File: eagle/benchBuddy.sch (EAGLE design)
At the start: 74 parts, among them IC2 TLC274D, IC3 LM334Z, IC4 LM324D, IC5 LM324D, J1 12V_DC, Q1 600mA/40V, U1 LP2983AIM5-1.0/NOPB, U2 LP2985-10DBVR

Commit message: Added all parts. Schematic finished. Consider Rev 1.0
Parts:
- added C10, C12, C14, C9: 10uF, rcl:C-USC0805
- added C11, C8: 0.1uF, rcl:C-USC0805
- added D1, D2, D3: (no value), SparkFun-LED:LED3MM
- added F1: 4A It, lab07lib:FUSE
- added F2, F3: 1.5A It, lab07lib:FUSE
- added J4, J8: GND, lab07lib:FAT-WIRE-TERM
- added J5: 3.3V, lab07lib:FAT-WIRE-TERM
- added J6: 5V, lab07lib:FAT-WIRE-TERM
- added J7: 12V, lab07lib:FAT-WIRE-TERM
- added J9: 0-10V, lab07lib:FAT-WIRE-TERM
- added PS1, PS2: P78E05-1000, P78E05-1000:P78E05-1000
- added R31, R32, R33: (no value), rcl:R-US_R1206
- added U3: 3V3REG, PowerManagementParts:3V3REG
- renumbered JP3 to J3, U$3 to J2
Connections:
- new net 3.3V: C10.1, C11.1, D3.A, J5.P$1, U3.VOUT
- new net 5V: C8.1, C9.1, D2.A, J3.6, J6.P$1, PS2.+VOUT/GND
- new net N$4: D1.A
- new net N$41: D1.C, R31.2
- new net N$42: D2.C, R32.2
- new net N$43: D3.C, R33.2
- new net N$44: F1.P$2, U$2.COM
- new net N$45: IC4B.OUT, LED3.A
- new net N$46: IC4C.OUT, LED4.A
- new net N$47: IC4D.OUT, LED5.A
- new net N$48: F2.P$1, PS1.+VOUT/GND
- new net N$49: C12.1, F2.P$2, U3.INPUT
- new net N$7: F3.P$2, PS2.+VIN
- net 10VOLTS: no longer J3.6
- net GND: now also C10.2, C11.2, C12.2, C14.2, C8.2, C9.2, J4.P$1, J8.P$1, PS1.GND/-VOUT, PS2.GND/-VOUT, R31.1, R32.1, R33.1, U3.GND
- net N$3: now also F1.P$1; no longer U$2.COM
- net VCC: now also J9.P$1
- net VIN: now also C14.1, F3.P$1, J7.P$1, PS1.+VIN
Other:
- note added: "1.0"
- note added: "3.3V @ 1A Supply"
- note added: "5V @ 1A Supply"
- note added: "Indicator LEDs"
- note added: "Mark Gilliland EENG 393 - ICE Field Session"
- note removed: "0.1"
- note removed: "Mark Gilliland 9/30/2019 EENG 393 - ICE Field Session"
- moved on the sheet: J1, U$2

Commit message: Basic dimensions and mechanical layout of board
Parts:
- renumbered U$2 to SW4
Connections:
- removed net N$4: D1.A
- net VIN: now also D1.A
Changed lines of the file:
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@@
 <part name="GND17" library="supply1" library_urn="urn:adsk.eagle:library:371" deviceset="GND" device=""/>
 <part name="U$1" library="lab07lib" deviceset="LT3080" device=""/>
-<part name="U$2" library="lab07lib" deviceset="EG2362" device=""/>
+<part name="SW4" library="lab07lib" deviceset="EG2362" device=""/>
 <part name="KK1" library="heatsink" library_urn="urn:adsk.eagle:library:236" deviceset="SK104-PAD" device="" package3d_urn="urn:adsk.eagle:package:14201/1"/>
 <part name="TP1" library="testpad" library_urn="urn:adsk.eagle:library:385" deviceset="TP" device="TP13R" package3d_urn="urn:adsk.eagle:package:27967/1"/>
@@
 </instance>
 <instance part="U$1" gate="G$1" x="177.8" y="185.42" smashed="yes"/>
-<instance part="U$2" gate="G$1" x="45.72" y="185.42" smashed="yes">
+<instance part="SW4" gate="G$1" x="45.72" y="185.42" smashed="yes">
 <attribute name="NAME" x="38.1" y="190.5" size="1.27" layer="94"/>
 <attribute name="VALUE" x="48.26" y="190.5" size="1.27" layer="94"/>
@@
 <junction x="63.5" y="182.88"/>
 <junction x="76.2" y="182.88"/>
-<pinref part="U$2" gate="G$1" pin="ON2"/>
+<pinref part="SW4" gate="G$1" pin="ON2"/>
 </segment>
 <segment>
@@
 <segment>
 <pinref part="F1" gate="G$1" pin="P$2"/>
-<pinref part="U$2" gate="G$1" pin="COM"/>
+<pinref part="SW4" gate="G$1" pin="COM"/>
 <wire x1="33.02" y1="185.42" x2="38.1" y2="185.42" width="0.1524" layer="91"/>
 </segment>
@@
 </busses>
 <nets>
-<net name="N$4" class="0">
-<segment>
-<pinref part="D1" gate="G$1" pin="A"/>
-<wire x1="45.72" y1="35.56" x2="45.72" y2="40.64" width="0.1524" layer="91"/>
-<pinref part="SUPPLY11" gate="G$1" pin="VIN"/>
-<wire x1="45.72" y1="40.64" x2="45.72" y2="38.1" width="0.1524" layer="91"/>
-</segment>
-</net>
 <net name="5V" class="0">
 <segment>
@@
 <wire x1="114.3" y1="20.32" x2="109.22" y2="20.32" width="0.1524" layer="91"/>
 </segment>
-</net>
+<segment>
+<pinref part="D1" gate="G$1" pin="A"/>
+<wire x1="45.72" y1="35.56" x2="45.72" y2="40.64" width="0.1524" layer="91"/>
+<pinref part="SUPPLY11" gate="G$1" pin="VIN"/>
+<wire x1="45.72" y1="40.64" x2="45.72" y2="38.1" width="0.1524" layer="91"/>
+</segment>
+</net>

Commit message: More detailed board layout. Began LED and VU layout
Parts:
- added C13: 0.1uF, rcl:C-USC0805
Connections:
- removed net N$22: C7.1, U2.VOUT
- removed net N$37: C5.1, U1.VOUT
- net 10VOLTS: now also C7.1, U2.VOUT
- net 1VOLT: now also C5.1, U1.VOUT
- net GND: now also C13.2
- net VCC: now also C13.1
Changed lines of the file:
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@@
 <part name="GND27" library="supply1" library_urn="urn:adsk.eagle:library:371" deviceset="GND" device=""/>
 <part name="SUPPLY12" library="SparkFun-PowerSymbols" library_urn="urn:adsk.eagle:library:530" deviceset="VIN" device=""/>
+<part name="C13" library="rcl" library_urn="urn:adsk.eagle:library:334" deviceset="C-US" device="C0805" package3d_urn="urn:adsk.eagle:package:23617/2" value="0.1uF"/>
 </parts>
 <sheets>
@@
 <attribute name="VALUE" x="25.4" y="188.722" size="1.778" layer="96"/>
 </instance>
+<instance part="C13" gate="G$1" x="223.52" y="175.26" smashed="yes">
+<attribute name="NAME" x="224.536" y="175.895" size="1.778" layer="95"/>
+<attribute name="VALUE" x="224.536" y="171.069" size="1.778" layer="96"/>
+</instance>
 </instances>
 <busses>
@@
 <pinref part="GND11" gate="1" pin="GND"/>
 <pinref part="C3" gate="G$1" pin="-"/>
-<wire x1="213.36" y1="162.56" x2="213.36" y2="170.18" width="0.1524" layer="91"/>
+<wire x1="213.36" y1="162.56" x2="213.36" y2="167.64" width="0.1524" layer="91"/>
+<pinref part="C13" gate="G$1" pin="2"/>
+<wire x1="213.36" y1="167.64" x2="213.36" y2="170.18" width="0.1524" layer="91"/>
+<wire x1="223.52" y1="170.18" x2="223.52" y2="167.64" width="0.1524" layer="91"/>
+<wire x1="223.52" y1="167.64" x2="213.36" y2="167.64" width="0.1524" layer="91"/>
+<junction x="213.36" y="167.64"/>
 </segment>
 <segment>
@@
 <wire x1="238.76" y1="182.88" x2="238.76" y2="187.96" width="0.1524" layer="91"/>
 <wire x1="213.36" y1="177.8" x2="213.36" y2="182.88" width="0.1524" layer="91"/>
-<wire x1="213.36" y1="182.88" x2="238.76" y2="182.88" width="0.1524" layer="91"/>
+<wire x1="213.36" y1="182.88" x2="223.52" y2="182.88" width="0.1524" layer="91"/>
 <junction x="238.76" y="182.88"/>
 <pinref part="U$1" gate="G$1" pin="VOUT"/>
+<wire x1="223.52" y1="182.88" x2="238.76" y2="182.88" width="0.1524" layer="91"/>
 <wire x1="213.36" y1="182.88" x2="203.2" y2="182.88" width="0.1524" layer="91"/>
 <junction x="213.36" y="182.88"/>
 <pinref part="J2" gate="G$1" pin="P$1"/>
 <wire x1="238.76" y1="182.88" x2="259.08" y2="182.88" width="0.1524" layer="91"/>
+<pinref part="C13" gate="G$1" pin="1"/>
+<wire x1="223.52" y1="177.8" x2="223.52" y2="182.88" width="0.1524" layer="91"/>
+<junction x="223.52" y="182.88"/>
 </segment>
 <segment>
@@
 <wire x1="246.38" y1="38.1" x2="226.06" y2="38.1" width="0.1524" layer="91"/>
 <label x="226.06" y="38.1" size="1.778" layer="95"/>
+</segment>
+<segment>
+<pinref part="U2" gate="A" pin="VOUT"/>
+<wire x1="243.84" y1="104.14" x2="261.62" y2="104.14" width="0.1524" layer="91"/>
+<pinref part="C7" gate="G$1" pin="1"/>
+<wire x1="261.62" y1="104.14" x2="261.62" y2="101.6" width="0.1524" layer="91"/>
+<junction x="261.62" y="104.14"/>
+<wire x1="261.62" y1="104.14" x2="266.7" y2="104.14" width="0.1524" layer="91"/>
+<label x="264.16" y="104.14" size="1.778" layer="95"/>
 </segment>
 </net>
@@
 <wire x1="243.84" y1="40.64" x2="226.06" y2="40.64" width="0.1524" layer="91"/>
 <label x="226.06" y="40.64" size="1.778" layer="95"/>
+</segment>
+<segment>
+<pinref part="C5" gate="G$1" pin="1"/>
+<wire x1="261.62" y1="127" x2="261.62" y2="129.54" width="0.1524" layer="91"/>
+<pinref part="U1" gate="A" pin="VOUT"/>
+<wire x1="261.62" y1="129.54" x2="243.84" y2="129.54" width="0.1524" layer="91"/>
+<wire x1="261.62" y1="129.54" x2="266.7" y2="129.54" width="0.1524" layer="91"/>
+<junction x="261.62" y="129.54"/>
+<label x="264.16" y="129.54" size="1.778" layer="95"/>
 </segment>
 </net>
@@
 </segment>
 </net>
-<net name="N$22" class="0">
-<segment>
-<pinref part="U2" gate="A" pin="VOUT"/>
-<wire x1="243.84" y1="104.14" x2="261.62" y2="104.14" width="0.1524" layer="91"/>
-<pinref part="C7" gate="G$1" pin="1"/>
-<wire x1="261.62" y1="104.14" x2="261.62" y2="101.6" width="0.1524" layer="91"/>
-</segment>
-</net>
-<net name="N$37" class="0">
-<segment>
-<pinref part="C5" gate="G$1" pin="1"/>
-<wire x1="261.62" y1="127" x2="261.62" y2="129.54" width="0.1524" layer="91"/>
-<pinref part="U1" gate="A" pin="VOUT"/>
-<wire x1="261.62" y1="129.54" x2="243.84" y2="129.54" width="0.1524" layer="91"/>
-</segment>
-</net>

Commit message: Most components in final position
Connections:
- net 10VOLTS: now also J3.6
- net 5V: no longer J3.6
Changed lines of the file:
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@@
 <label x="264.16" y="104.14" size="1.778" layer="95"/>
+</segment>
+<segment>
+<pinref part="J3" gate="A" pin="6"/>
+<wire x1="152.4" y1="55.88" x2="175.26" y2="55.88" width="0.1524" layer="91"/>
+<label x="167.64" y="55.88" size="1.778" layer="95"/>
 </segment>
 </net>
@@
 </segment>
 </net>
-<net name="5V" class="0">
-<segment>
-<pinref part="J3" gate="A" pin="6"/>
-<wire x1="152.4" y1="55.88" x2="175.26" y2="55.88" width="0.1524" layer="91"/>
-<label x="172.72" y="55.88" size="1.778" layer="95"/>
-</segment>
-</net>

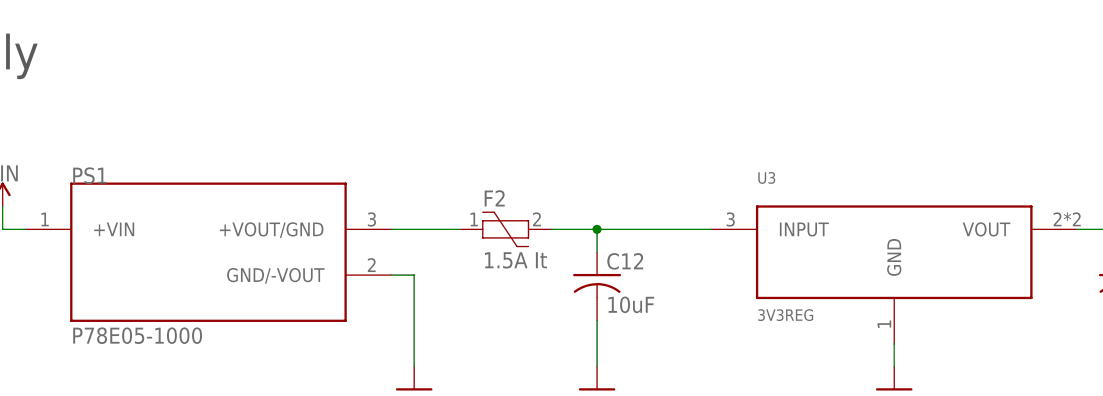
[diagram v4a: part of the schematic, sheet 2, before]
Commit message: Added mini heatsinks for T220 Packages. Also more work on layout
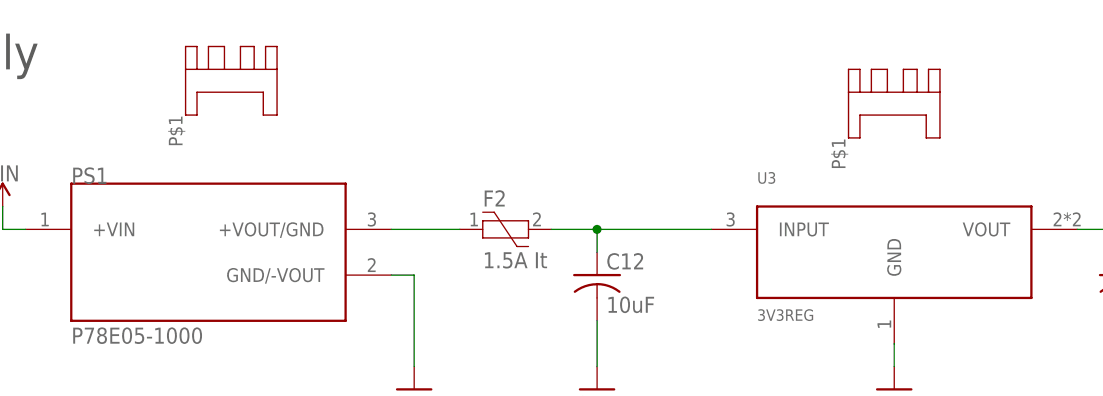
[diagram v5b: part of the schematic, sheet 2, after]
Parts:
- added U$2, U$3: HEATSINK_MINI, lab07lib:HEATSINK_MINI
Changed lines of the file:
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@@
 <part name="SUPPLY12" library="SparkFun-PowerSymbols" library_urn="urn:adsk.eagle:library:530" deviceset="VIN" device=""/>
 <part name="C13" library="rcl" library_urn="urn:adsk.eagle:library:334" deviceset="C-US" device="C0805" package3d_urn="urn:adsk.eagle:package:23617/2" value="0.1uF"/>
+<part name="U$2" library="lab07lib" deviceset="HEATSINK_MINI" device=""/>
+<part name="U$3" library="lab07lib" deviceset="HEATSINK_MINI" device=""/>
 </parts>
 <sheets>
@@
 <attribute name="VALUE" x="106.68" y="23.114" size="1.778" layer="96" align="center-right"/>
 </instance>
+<instance part="U$2" gate="G$1" x="66.04" y="198.12" smashed="yes"/>
+<instance part="U$3" gate="G$1" x="139.7" y="195.58" smashed="yes"/>
 </instances>
 <busses>

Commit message: Board mostly routed! Added heatsink 3.3V version
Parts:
- U3: value 3V3REG -> 3V3REG-HEATSINK; device PowerManagementParts:3V3REG -> lab07lib:3V3REG-HEATSINK
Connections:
- net I_SET_MICRO: now also J3.4; no longer J3.3
- net VCC: now also J3.3; no longer J3.4
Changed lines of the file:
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@@
 <part name="D2" library="SparkFun-LED" library_urn="urn:adsk.eagle:library:529" deviceset="LED" device="3MM" package3d_urn="urn:adsk.eagle:package:39361/1"/>
 <part name="D3" library="SparkFun-LED" library_urn="urn:adsk.eagle:library:529" deviceset="LED" device="3MM" package3d_urn="urn:adsk.eagle:package:39361/1"/>
-<part name="U3" library="PowerManagementParts" deviceset="3V3REG" device="" package3d_urn="urn:adsk.eagle:package:43439/1"/>
+<part name="U3" library="lab07lib" deviceset="3V3REG" device="-HEATSINK"/>
 <part name="R31" library="rcl" library_urn="urn:adsk.eagle:library:334" deviceset="R-US_" device="R1206" package3d_urn="urn:adsk.eagle:package:23540/2"/>
 <part name="R32" library="rcl" library_urn="urn:adsk.eagle:library:334" deviceset="R-US_" device="R1206" package3d_urn="urn:adsk.eagle:package:23540/2"/>
@@
 </segment>
 <segment>
-<pinref part="J3" gate="A" pin="4"/>
-<wire x1="152.4" y1="50.8" x2="175.26" y2="50.8" width="0.1524" layer="91"/>
-<label x="170.18" y="50.8" size="1.778" layer="95"/>
+<pinref part="J3" gate="A" pin="3"/>
+<wire x1="152.4" y1="48.26" x2="167.64" y2="48.26" width="0.1524" layer="91"/>
+<label x="167.64" y="48.26" size="1.778" layer="95"/>
 </segment>
 </net>
@@
 <net name="I_SET_MICRO" class="0">
 <segment>
-<pinref part="J3" gate="A" pin="3"/>
-<wire x1="152.4" y1="48.26" x2="167.64" y2="48.26" width="0.1524" layer="91"/>
-<label x="160.02" y="48.26" size="1.778" layer="95"/>
-</segment>
-<segment>
 <pinref part="S3" gate="G$1" pin="4"/>
 <wire x1="127" y1="124.46" x2="109.22" y2="124.46" width="0.1524" layer="91"/>
 <label x="109.22" y="124.46" size="1.778" layer="95"/>
 </segment>
+<segment>
+<pinref part="J3" gate="A" pin="4"/>
+<wire x1="152.4" y1="50.8" x2="175.26" y2="50.8" width="0.1524" layer="91"/>
+<label x="165.1" y="50.8" size="1.778" layer="95"/>
+</segment>
 </net>
 <net name="V_SET_MICRO" class="0">
-<segment>
-<pinref part="J3" gate="A" pin="5"/>
-<wire x1="152.4" y1="53.34" x2="167.64" y2="53.34" width="0.1524" layer="91"/>
-<label x="160.02" y="53.34" size="1.778" layer="95"/>
-</segment>
 <segment>
 <pinref part="S3" gate="G$1" pin="1"/>
 <wire x1="127" y1="116.84" x2="109.22" y2="116.84" width="0.1524" layer="91"/>
 <label x="109.22" y="116.84" size="1.778" layer="95"/>
+</segment>
+<segment>
+<pinref part="J3" gate="A" pin="5"/>
+<wire x1="152.4" y1="53.34" x2="167.64" y2="53.34" width="0.1524" layer="91"/>
+<label x="165.1" y="53.34" size="1.778" layer="95"/>
 </segment>
 </net>
@@
 </instance>
 <instance part="U$2" gate="G$1" x="66.04" y="198.12" smashed="yes"/>
-<instance part="U$3" gate="G$1" x="139.7" y="195.58" smashed="yes"/>
+<instance part="U$3" gate="G$1" x="78.74" y="142.24" smashed="yes"/>
 </instances>
 <busses>

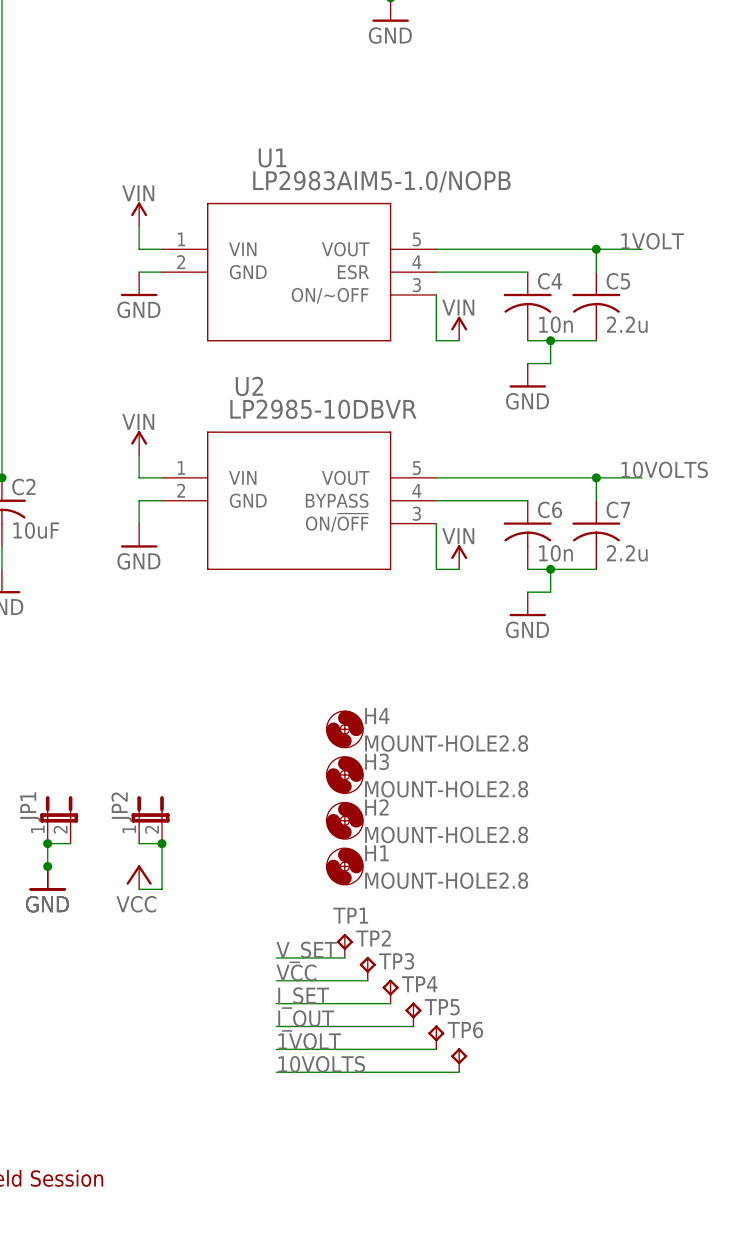
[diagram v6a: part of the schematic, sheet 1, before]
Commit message: Board fully routed. Added test header
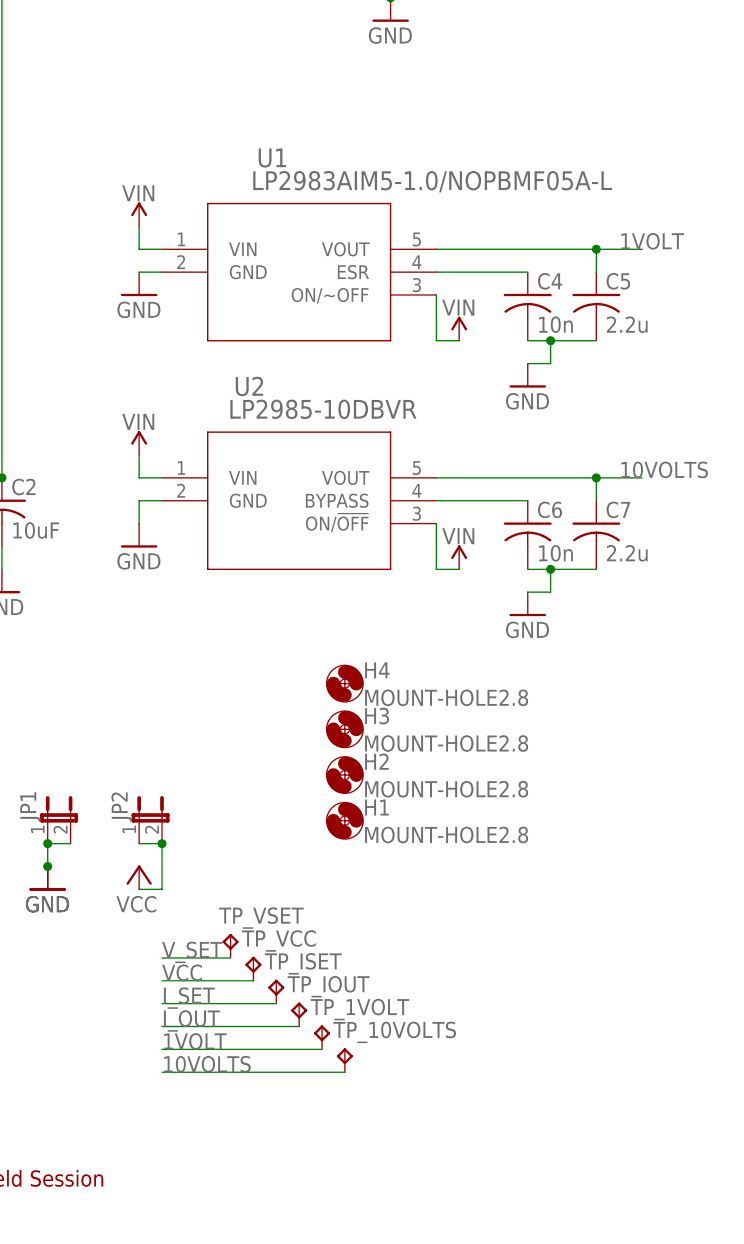
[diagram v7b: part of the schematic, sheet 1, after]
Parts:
- removed TP1, TP2, TP3, TP4, TP5, TP6: TPTP13R, testpad:TPTP13R
- added TEST_PADS: (no value), SparkFun-Connectors:CONN_03X2NO_SILK
- added TP_10VOLTS, TP_1VOLT, TP_IOUT, TP_ISET, TP_VCC, TP_VSET: TPB1,27, testpad:TPB1,27
- U1: value LP2983AIM5-1.0/NOPB -> LP2983AIM5-1.0/NOPBMF05A-L; device lab07lib:LP2983AIM5-1.0/NOPB -> lab07lib:LP2983AIM5-1.0/NOPBMF05A-L
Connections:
- net 10VOLTS: now also TEST_PADS.5, TP_10VOLTS.TP; no longer TP6.TP
- net 1VOLT: now also TEST_PADS.6, TP_1VOLT.TP; no longer TP5.TP
- net I_OUT: now also TEST_PADS.1, TP_IOUT.TP; no longer TP4.TP
- net I_SET: now also TEST_PADS.2, TP_ISET.TP; no longer TP3.TP
- net VCC: now also TEST_PADS.3, TP_VCC.TP; no longer TP2.TP
- net V_SET: now also TEST_PADS.4, TP_VSET.TP; no longer TP1.TP
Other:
- moved on the sheet: H1, H2, H3, H4

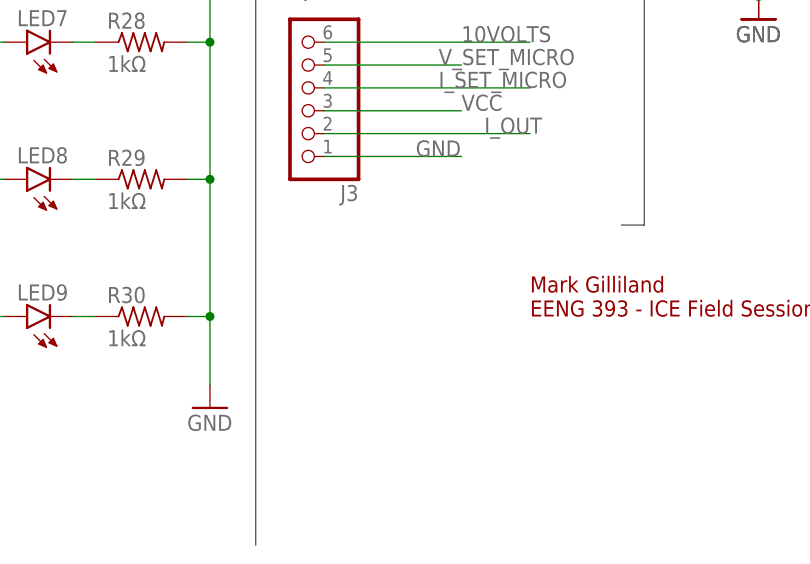
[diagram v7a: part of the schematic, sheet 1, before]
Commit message: Minimized board area to 4.5x3inches
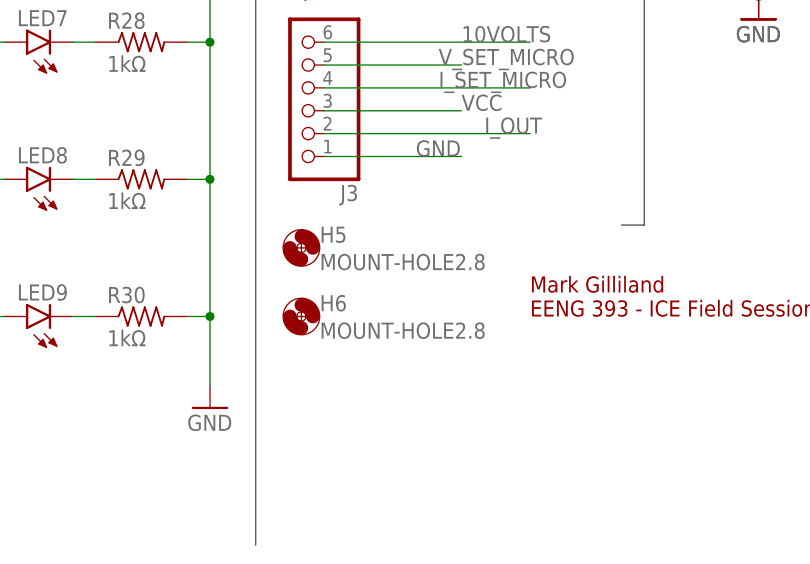
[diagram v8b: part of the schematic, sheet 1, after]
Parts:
- added H5, H6: MOUNT-HOLE2.8, holes:MOUNT-HOLE2.8
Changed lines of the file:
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@@
 <part name="U$3" library="lab07lib" deviceset="HEATSINK_MINI" device=""/>
 <part name="TEST_PADS" library="SparkFun-Connectors" library_urn="urn:adsk.eagle:library:513" deviceset="CONN_03X2" device="NO_SILK" package3d_urn="urn:adsk.eagle:package:38013/1"/>
+<part name="H5" library="holes" library_urn="urn:adsk.eagle:library:237" deviceset="MOUNT-HOLE" device="2.8" package3d_urn="urn:adsk.eagle:package:14271/1"/>
+<part name="H6" library="holes" library_urn="urn:adsk.eagle:library:237" deviceset="MOUNT-HOLE" device="2.8" package3d_urn="urn:adsk.eagle:package:14271/1"/>
 </parts>
 <sheets>
@@
 <attribute name="VALUE" x="224.536" y="171.069" size="1.778" layer="96"/>
 </instance>
+<instance part="H5" gate="G$1" x="149.86" y="33.02" smashed="yes">
+<attribute name="NAME" x="151.892" y="33.6042" size="1.778" layer="95"/>
+<attribute name="VALUE" x="151.892" y="30.5562" size="1.778" layer="96"/>
+</instance>
+<instance part="H6" gate="G$1" x="149.86" y="25.4" smashed="yes">
+<attribute name="NAME" x="151.892" y="25.9842" size="1.778" layer="95"/>
+<attribute name="VALUE" x="151.892" y="22.9362" size="1.778" layer="96"/>
+</instance>
 </instances>
